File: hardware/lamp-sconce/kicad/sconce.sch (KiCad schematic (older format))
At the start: 28 parts

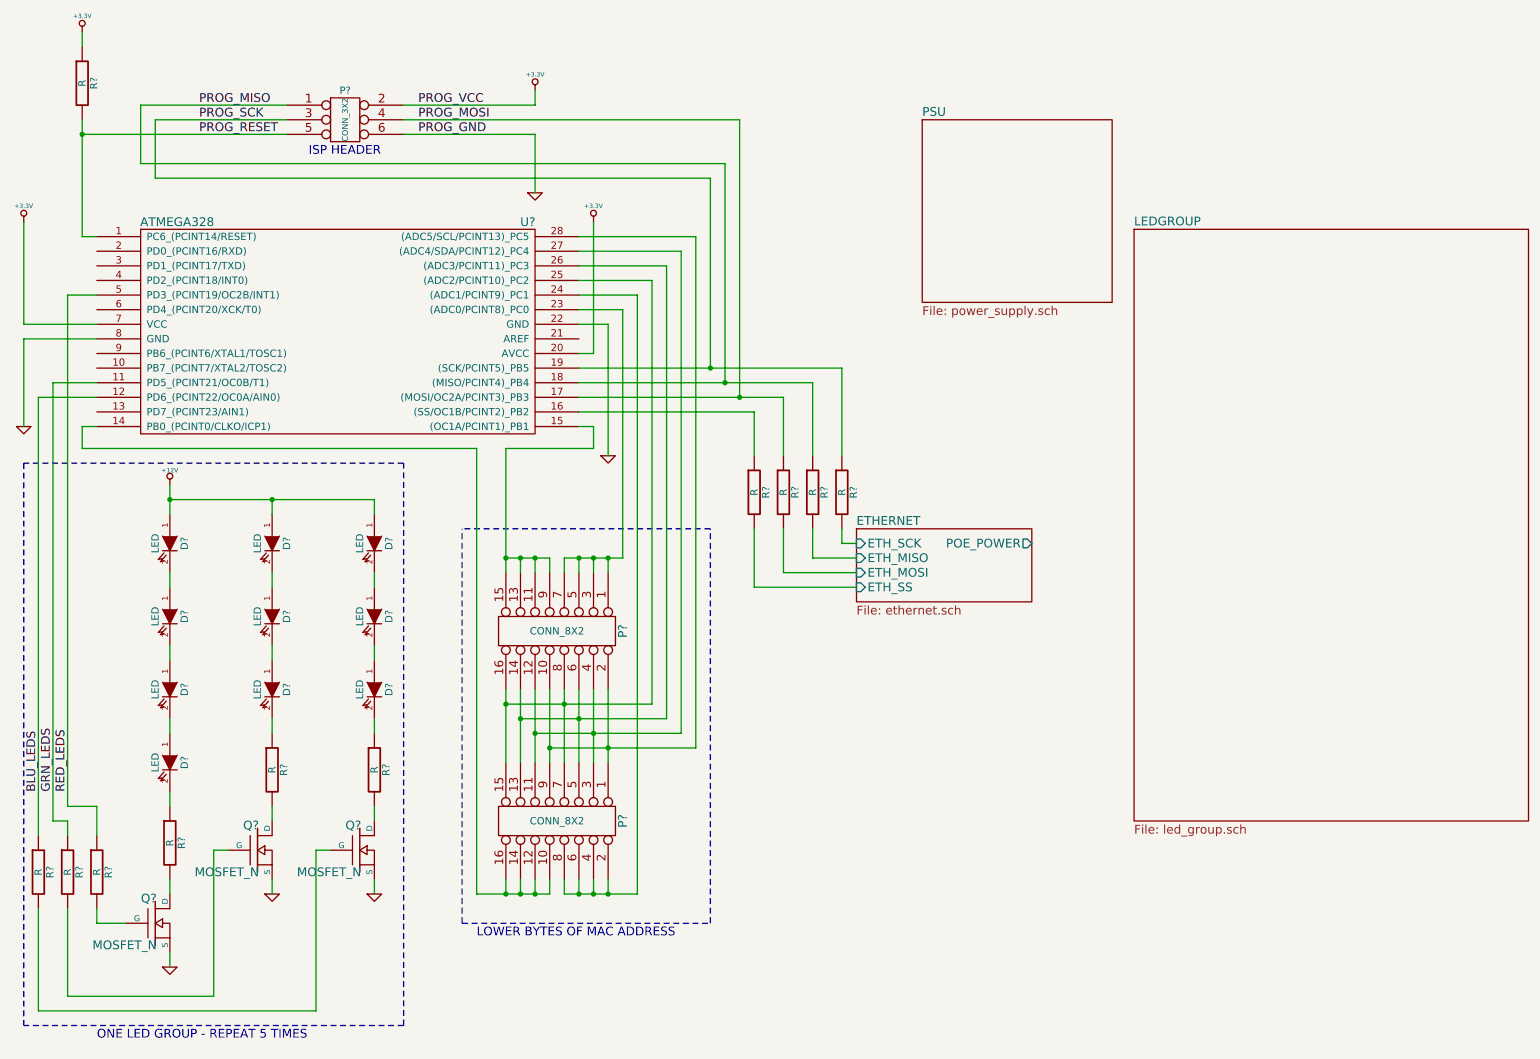
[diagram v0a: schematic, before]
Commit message: Adding more work for the sconce lamp.  Schematic is pretty much complete.
Signed-off-by: Daniel P Williams <dwilliams@port8080.net>
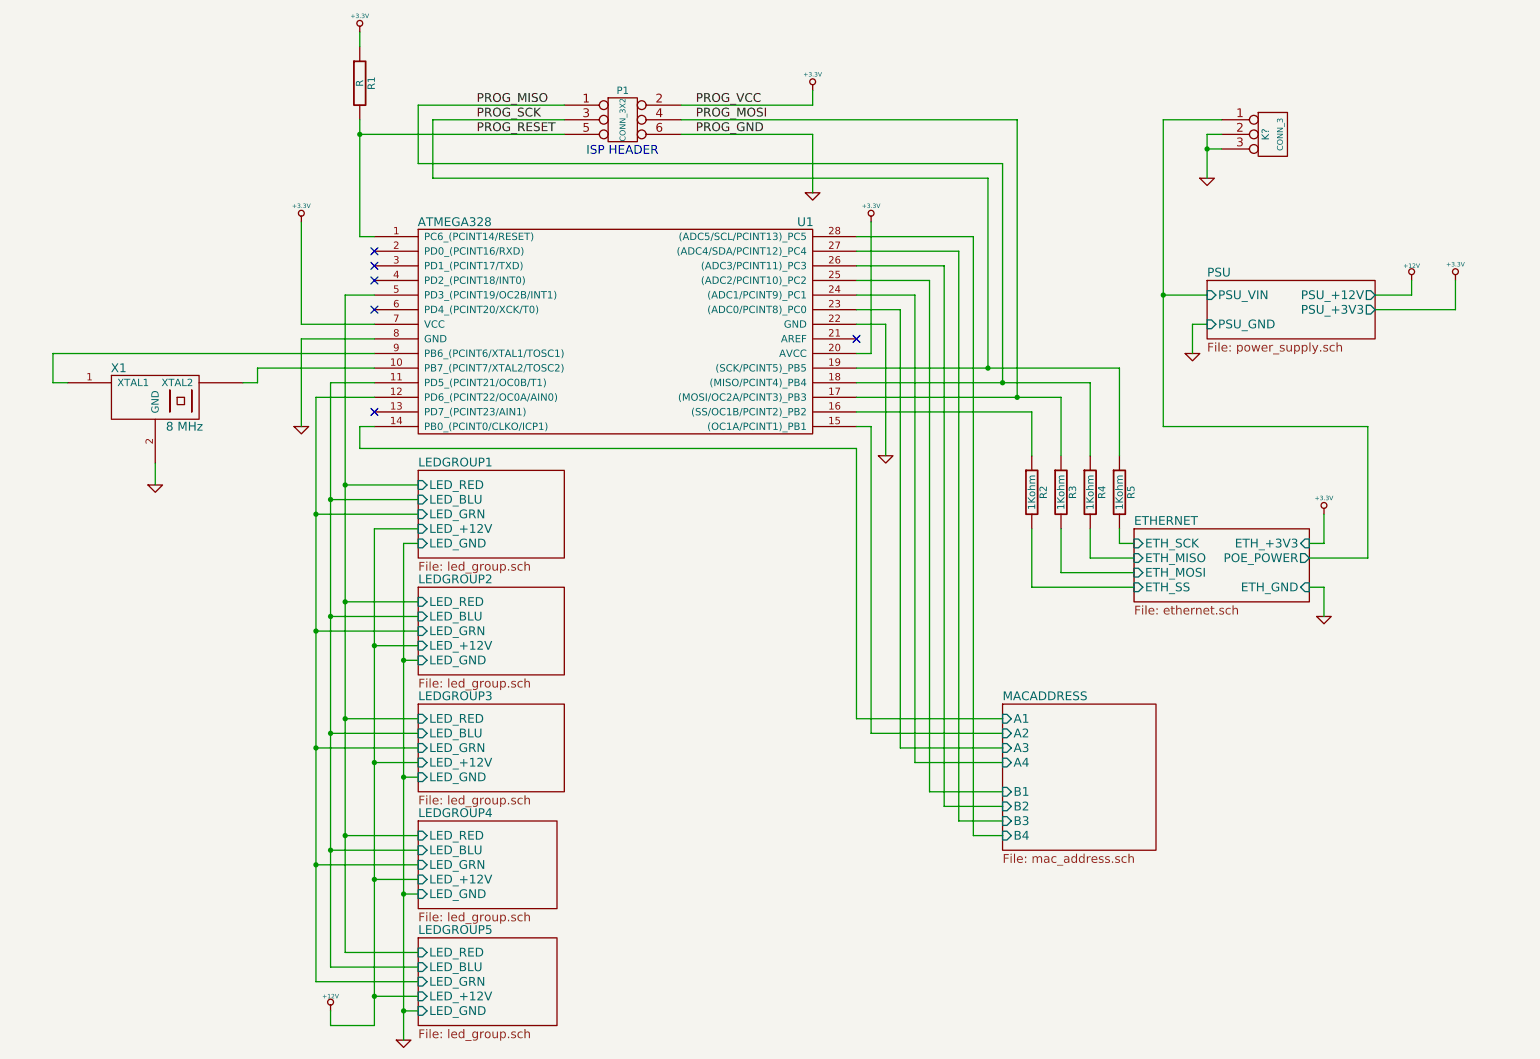
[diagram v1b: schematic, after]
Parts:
- removed D? (x10): LED, symbol LED
- removed P? (x2): CONN_8X2, symbol CONN_8X2
- removed Q? (x3): MOSFET_N, symbol MOSFET_N
- removed R? (x6): R, symbol R
- added K?: CONN_3, symbol CONN_3
- added X1: 8 MHz, symbol XRES
- R2, R3, R4, R5: renamed from R?; value R -> 1Kohm; Digi-Key Part (none) -> RMCF1206JT1K00CT-ND
- gave numbers to parts that had none: 3
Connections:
- net ETHERNET/POE_POWER: now also K?.1 (P1)
- net GND: now also K?.2 (PM), K?.3 (P3), X1.2 (GND)
- net at U1.10 (PB7_(PCINT7/XTAL2/TOSC2)): now also X1.~ (XTAL2)
- net MACADDRESS/A1: now reaches U1.14 (PB0_(PCINT0/CLKO/ICP1))
- net MACADDRESS/A2: now reaches U1.15 ((OC1A/PCINT1)_PB1)
- net MACADDRESS/A3: now reaches U1.23 ((ADC0/PCINT8)_PC0)
- net MACADDRESS/A4: now reaches U1.24 ((ADC1/PCINT9)_PC1)
- net MACADDRESS/B1: now reaches U1.25 ((ADC2/PCINT10)_PC2)
- net MACADDRESS/B2: now reaches U1.26 ((ADC3/PCINT11)_PC3)
- net MACADDRESS/B3: now reaches U1.27 ((ADC4/SDA/PCINT12)_PC4)
- net MACADDRESS/B4: now reaches U1.28 ((ADC5/SCL/PCINT13)_PC5)
- net at U1.9 (PB6_(PCINT6/XTAL1/TOSC1)): now also X1.1 (XTAL1)
- net BLU_LEDS renamed LEDGROUP1/LED_GRN
- net GRN_LEDS renamed LEDGROUP1/LED_BLU
- net RED_LEDS renamed LEDGROUP1/LED_RED
- no-connect marks 0 -> 6
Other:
- note removed: "LOWER BYTES OF MAC ADDRESS"
- note removed: "ONE LED GROUP - REPEAT 5 TIMES"
- moved on the sheet: P1, R1, R2, R3, R4, R5, U1
